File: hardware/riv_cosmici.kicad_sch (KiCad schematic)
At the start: 66 parts, among them J1 SiPM, J2 TTL_OUT, J3 PWR_5V, J4 LEMO_OUT, Q1 BFR93A, Q2 MMBTH81, Q3 MMBT2222A, Q4 MMBT2222A, U1 LT3461, U2 TLC555/LMC555, U3 MAX961, U4 MCP1402, U5 LP2985AIM5-3.6, U6 MCP1825S-3302, U7 LP2985AIM5-3.6, U8 LT1636

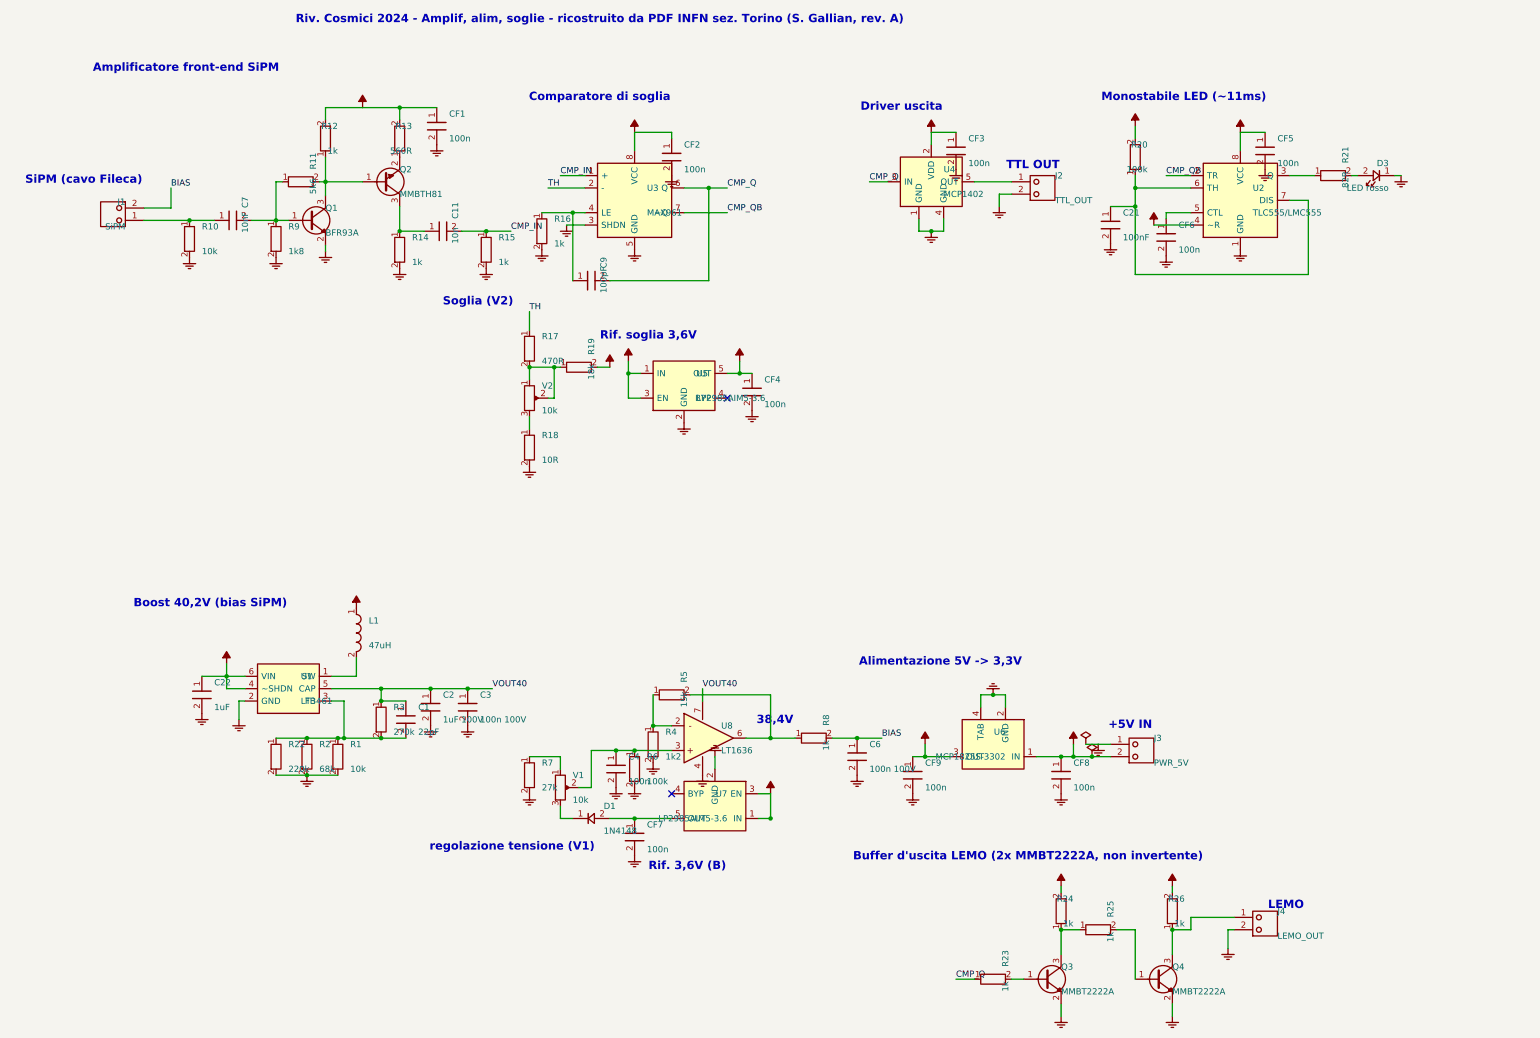
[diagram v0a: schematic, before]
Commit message: Scheda completa: simulazione LTspice, correzione V2, uscita 3,3 V per Raspberry Pi
- Schema KiCad confrontato pin per pin con l'originale INFN: V2 e' un
  potenziometro (cursore -> R17 -> TH), non un reostato. Corretto.
- Uscita J4 per Raspberry Pi: il buffer a 2 transistor a 5 V (lento,
  uscita fino a -0,7 V, 5 V sui GPIO) sostituito da U9 74LVC1G17 a +3V3
  + R23 33 ohm. Buffer ora anche su PCB e Gerber.
- PCB rigenerato (autorouter con rip-up & retry): 0 errori DRC e
  connettivita'. Gerber + zip, anteprime, riv.kicad_sym, BOM generata
  da netdata.py (gen_bom.py).
- simulation/ltspice/: scheda intera come schema LTspice (.asc + .asy)
  e netlist (.cir), generati dallo stesso modello dati del KiCad;
  macromodelli di tutti gli integrati; verifica_ltspice.py controlla
  .asc == .cir e 21 grandezze con ngspice (tutte OK).
- netlist_from_kicad: PWR_FLAG non e' piu' trattato come una rete.
- hardware/PRIMA_DI_ORDINARE.md: verifiche fatte e punti da decidere
  al montaggio (R3/limite 40 V LT3461, condensatori LDO, L1, LEMO).

Co-Authored-By: Claude Opus 5.5 <noreply@anthropic.com>
Claude-Session: https://claude.ai/code/session_017fc9yPsNewCQrMK8R1c8Ls
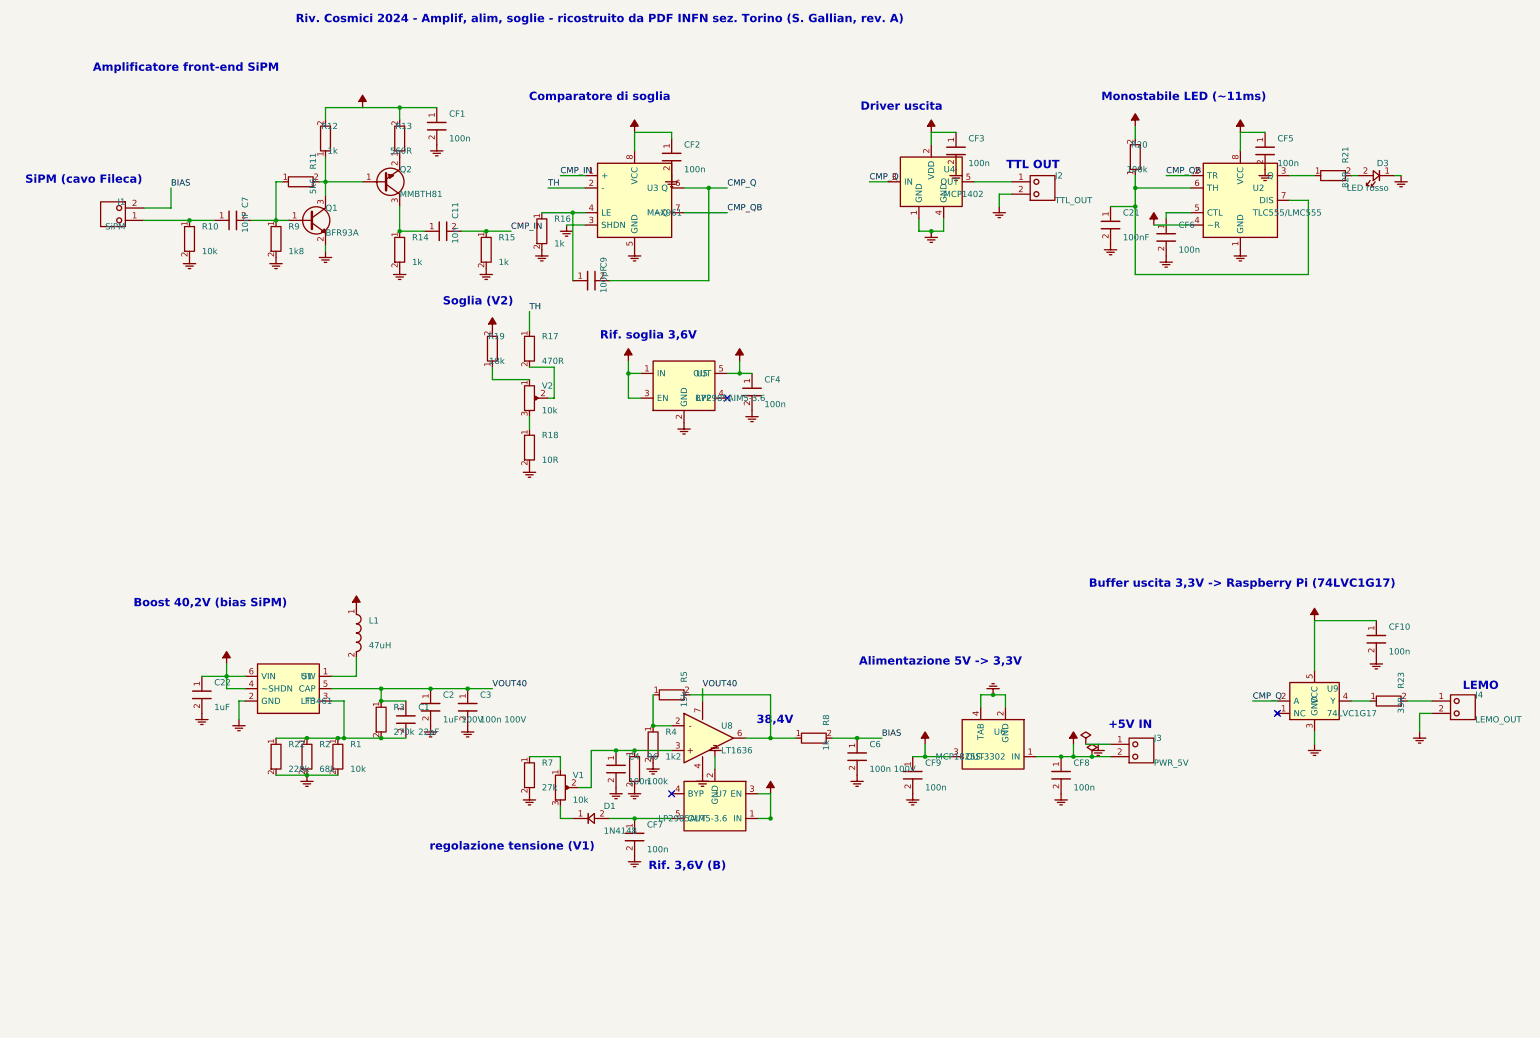
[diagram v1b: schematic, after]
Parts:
- removed Q3, Q4: MMBT2222A, rivlib:SOT23, symbol riv:NPN
- removed R24, R25, R26: 1k, rivlib:R_0805, symbol riv:R
- added CF10: 100n, rivlib:C_0805, symbol riv:C
- added U9: 74LVC1G17, rivlib:SOT23-5, symbol riv:LVC1G17
- R23: value 1k -> 33R
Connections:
- net +3V3: now also CF10.1, U9.5 (VCC)
- net CMP_Q: now also U9.2 (A); no longer R23.1
- net GND: now also CF10.2, U9.3 (GND)
- net at R23.2: now also J4.1
- net at R17.2, V2.2 (W): no longer R19.1, V2.1
- new net: R23.1, U9.4 (Y)
- new net: R19.1, V2.1
- no-connect marks 2 -> 3
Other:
- note added: "Buffer uscita 3,3V -> Raspberry Pi (74LVC1G17)"
- note removed: "Buffer d'uscita LEMO (2x MMBT2222A, non invertente)"

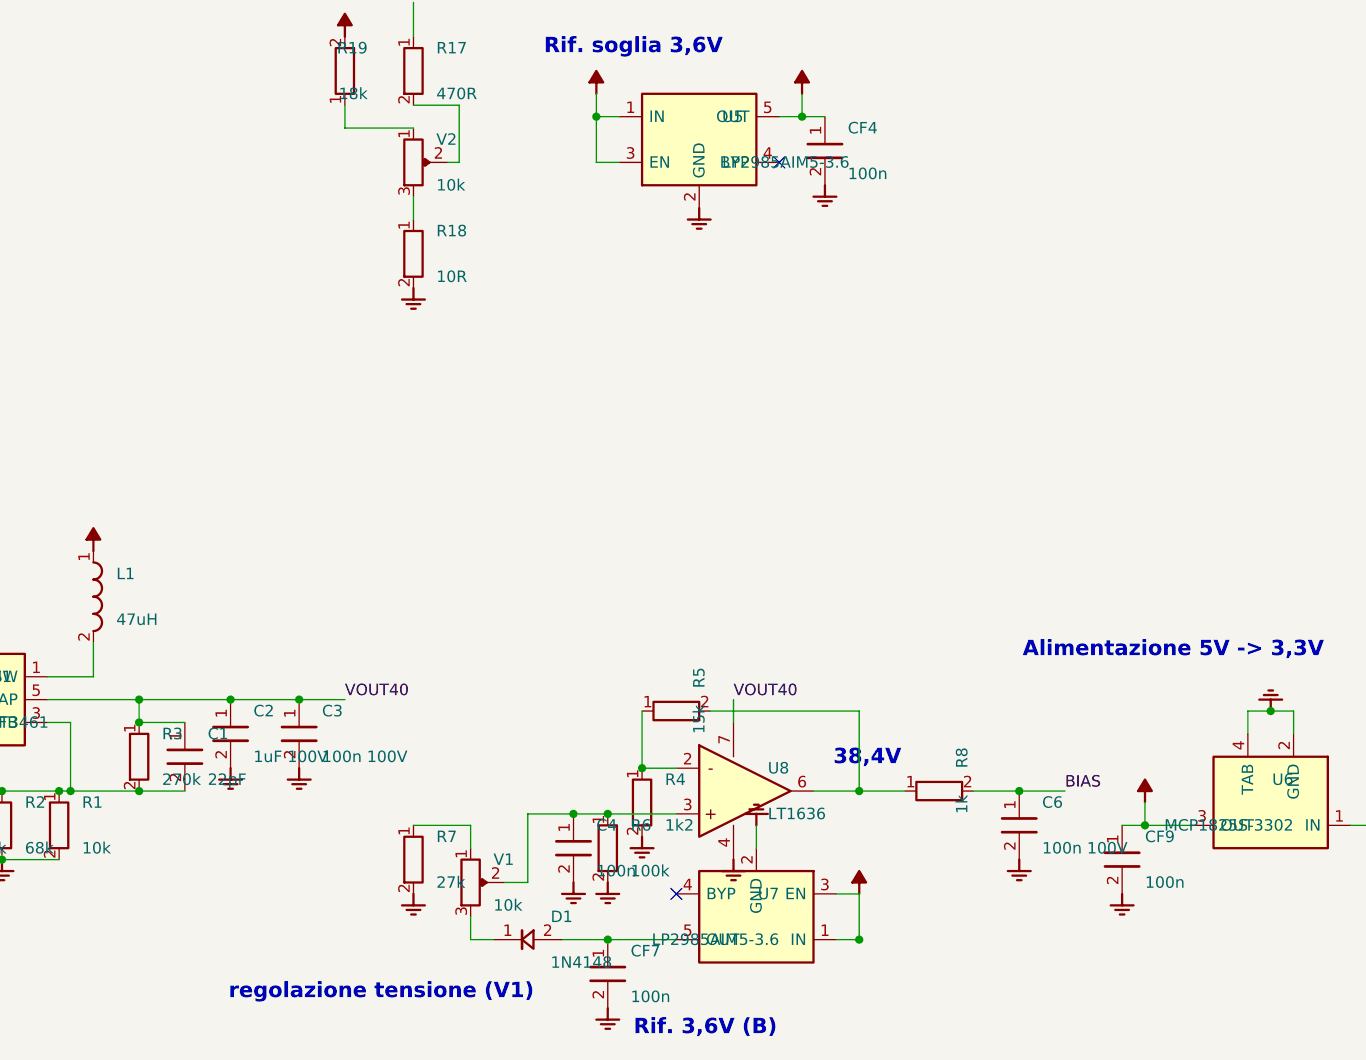
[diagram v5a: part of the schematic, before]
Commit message: R3 = 255k e 2,2 uF su CF4/CF7/CF9 (datasheet LT3461, LP2985, MCP1825), nota per la verifica INFN
- R3 270k -> 255k: VOUT40 da 41,7 a 39,4 V, sotto i 40 V max assoluti del LT3461;
  bias ancora regolabile fino a ~39,2 V (margine 1,0 V a 25 C, 0,3 V a 50 C).
- CF4, CF7, CF9 100n -> 2,2 uF X7R 0805 (Samsung CL21B225KAFNNNE): uscite dei
  regolatori, come richiesto dai datasheet.
- Schemi, PCB (valori), BOM, file JLCPCB, PDF, simulazioni e render rigenerati;
  verifica_ltspice: tutto OK; sim_3canali invariata salvo VOUT40.
- hardware/variante_3ch/NOTA_PER_TECNICO_INFN.txt: le due modifiche con calcoli,
  simulazioni e punti da verificare, piu' l'elenco delle differenze dalla scheda INFN.

Co-Authored-By: Claude Opus 5.5 <noreply@anthropic.com>
Claude-Session: https://claude.ai/code/session_017fc9yPsNewCQrMK8R1c8Ls
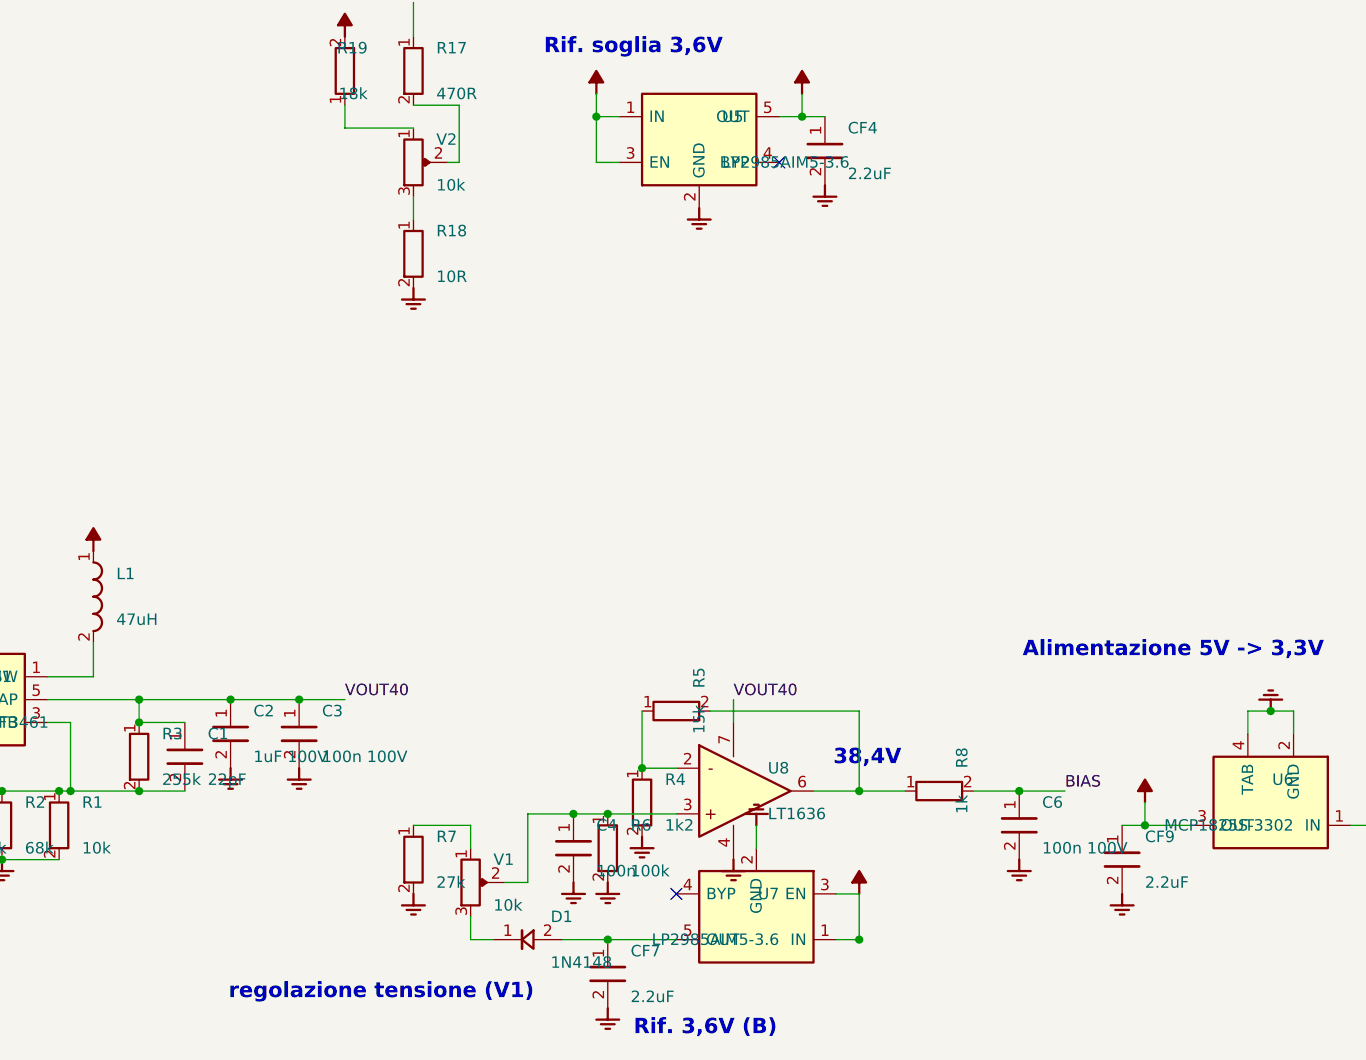
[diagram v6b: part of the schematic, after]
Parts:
- CF4, CF7, CF9: value 100n -> 2.2uF
- R3: value 270k -> 255k
